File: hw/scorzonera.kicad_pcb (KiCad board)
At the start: 4 copper layers, 70.7 x 53.3 mm, 7 parts, among them J1 NEIGHBOR1, J2 NEIGHBOR2, J7 BONUS_ROW

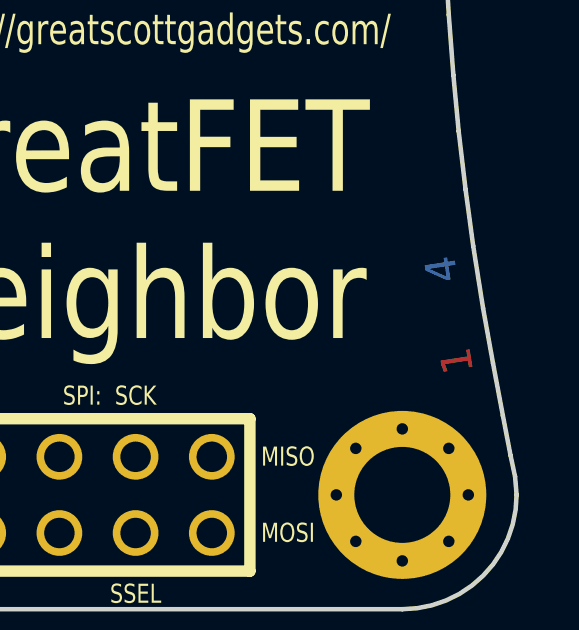
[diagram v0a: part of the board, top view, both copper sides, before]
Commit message: Switch to 2 layer
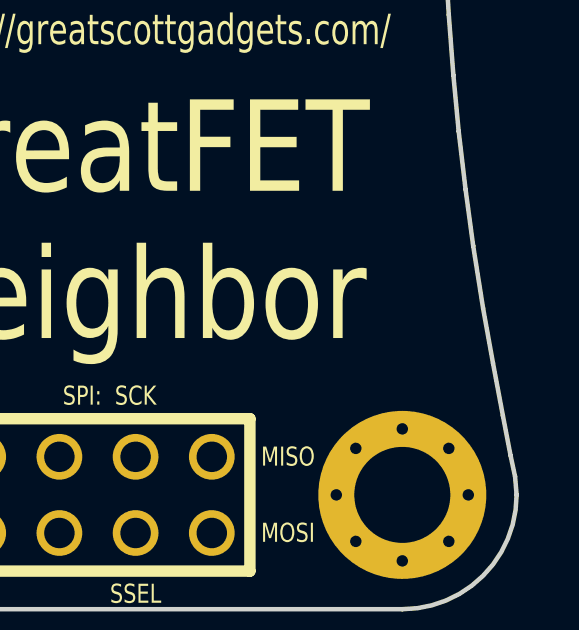
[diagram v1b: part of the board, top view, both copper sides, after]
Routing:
- removed copper zone on C2.Cu, net GND
- removed copper zone on C3.Cu, net VCC
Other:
- copper layers 4 -> 2
- board text removed: "1"
- board text removed: "2"
- board text removed: "3"
- board text removed: "4"
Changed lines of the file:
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@@
-(kicad_pcb (version 4) (host pcbnew 4.0.6)
+(kicad_pcb (version 20171130) (host pcbnew 5.0.2-bee76a0~70~ubuntu18.04.1)
   (general
-    (links 41)
-    (no_connects 0)
-    (area 107.95 66.04 279.525801 124.460001)
     (thickness 1.6)
-    (drawings 122)
+    (drawings 118)
     (tracks 0)
     (zones 0)
@@
   (layers
     (0 F.Cu signal)
-    (1 C2.Cu power)
-    (2 C3.Cu power)
     (31 B.Cu signal)
     (32 B.Adhes user)
@@
     (pad_drill 0.762)
     (pad_to_mask_clearance 0.127)
+    (solder_mask_min_width 0.25)
     (pad_to_paste_clearance_ratio -0.05)
     (aux_axis_origin 0 0)
@@
       (layerselection 0x010fc_80000007)
       (usegerberextensions true)
+      (usegerberattributes false)
+      (usegerberadvancedattributes false)
+      (creategerberjobfile false)
       (excludeedgelayer true)
       (linewidth 0.100000)
@@
       (hpglpennumber 1)
       (hpglpenspeed 20)
-      (hpglpendiameter 15)
-      (hpglpenoverlay 2)
+      (hpglpendiameter 15.000000)
       (psnegative false)
       (psa4output false)
@@
       (drillshape 0)
       (scaleselection 1)
-      (outputdirectory gerber))
+      (outputdirectory "gerber"))
   )
   (net 0 "")
@@
   (gr_text "27 September 2015" (at 153.4414 114.4016) (layer F.SilkS)
     (effects (font (size 1.016 0.762) (thickness 0.1524)))
-  )
-  (gr_text 4 (at 177.8508 110.5916 98.9) (layer B.Cu)
-    (effects (font (size 1.016 1.016) (thickness 0.1778)))
-  )
-  (gr_text 3 (at 178.0286 111.633 98.9) (layer C3.Cu)
-    (effects (font (size 1.016 1.016) (thickness 0.1778)))
-  )
-  (gr_text 2 (at 178.181 112.6236 98.9) (layer C2.Cu)
-    (effects (font (size 1.016 1.016) (thickness 0.1778)))
-  )
-  (gr_text 1 (at 178.3588 113.6396 98.9) (layer F.Cu)
-    (effects (font (size 1.016 1.016) (thickness 0.1778)))
   )
   (gr_text https://greatscottgadgets.com/ (at 168.021 102.616) (layer F.SilkS)
@@
   (gr_line (start 176.53 121.92) (end 116.1288 121.92) (angle 90) (layer Edge.Cuts) (width 0.15))
   (gr_line (start 116.1288 68.58) (end 176.53 68.58) (angle 90) (layer Edge.Cuts) (width 0.15))
-  (zone (net 2) (net_name VCC) (layer C3.Cu) (hatch edge 0.508)
-    (connect_pads (clearance 0.254))
-    (min_thickness 0.254)
-    (fill yes (arc_segments 16) (thermal_gap 0.254) (thermal_bridge_width 0.508))
-    (polygon
-      (pts
-        (xy 107.95 66.04) (xy 181.61 66.04) (xy 181.5084 109.0422) (xy 176.2506 109.8296) (xy 177.1142 114.7826)
-        (xy 181.61 114.0714) (xy 181.61 124.46) (xy 107.95 124.46)
-      )
-    )
-  )
-  (zone (net 1) (net_name GND) (layer C2.Cu) (hatch edge 0.508)
-    (connect_pads (clearance 0.254))
-    (min_thickness 0.254)
-    (fill yes (arc_segments 16) (thermal_gap 0.254) (thermal_bridge_width 0.508))
-    (polygon
-      (pts
-        (xy 107.95 66.04) (xy 181.61 66.04) (xy 181.5084 109.0422) (xy 176.2506 109.8296) (xy 177.1142 114.7826)
-        (xy 181.6354 114.0714) (xy 181.61 124.46) (xy 107.95 124.46)
-      )
-    )
-  )
 )

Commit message: Update silk
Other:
- board text added: "5 May 2019"
- board text added: "Scorzonera"
- board text added: "https://flomp.net/scorzonera"
- board text removed: "27 September 2015"
- board text removed: "GreatFET Neighbor"
- board text removed: "https://greatscottgadgets.com/"
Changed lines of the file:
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@@
   (gr_line (start 177.9016 92.3544) (end 177.8508 94.0054) (angle 90) (layer Edge.Cuts) (width 0.15))
   (gr_line (start 177.9524 90.5002) (end 177.9016 92.3544) (angle 90) (layer Edge.Cuts) (width 0.15))
-  (gr_text "27 September 2015" (at 153.4414 114.4016) (layer F.SilkS)
+  (gr_text "5 May 2019" (at 153.4414 114.4016) (layer F.SilkS)
     (effects (font (size 1.016 0.762) (thickness 0.1524)))
   )
-  (gr_text https://greatscottgadgets.com/ (at 168.021 102.616) (layer F.SilkS)
+  (gr_text https://flomp.net/scorzonera (at 168.1 105.3) (layer F.SilkS)
     (effects (font (size 1.016 0.762) (thickness 0.1524)))
   )
@@
   (gr_arc (start 176.53 118.11) (end 180.34 118.11) (angle 90) (layer Edge.Cuts) (width 0.15))
   (gr_arc (start 279.4508 95.25) (end 177.8508 95.25) (angle 12.5) (layer Cmts.User) (width 0.15))
-  (gr_text "GreatFET\nNeighbor" (at 167.386 109.0168) (layer F.SilkS)
+  (gr_text Scorzonera (at 167.386 109.0168) (layer F.SilkS)
     (effects (font (size 3.048 2.54) (thickness 0.4572)))
   )

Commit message: Some wiring
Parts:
- added U1: AM7969, Package_LCC:PLCC-28, F.Cu at (146.1, 92.1)
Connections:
- net /VBUS renamed Net-(J2-Pad2)
- J1 pad 10: (no net) -> /P1_1
- J1 pad 11: (no net) -> /CLK0
- J1 pad 12: (no net) -> /P1_2
- J1 pad 13: (no net) -> /P1_5
- J1 pad 14: (no net) -> /P5_2
- J1 pad 15: (no net) -> /P1_7
- J1 pad 16: (no net) -> /P1_6
- J1 pad 17: (no net) -> /P1_9
- J1 pad 18: (no net) -> /P1_8
- J1 pad 19: (no net) -> /P5_3
- J1 pad 20: (no net) -> /P1_10
- J1 pad 21: (no net) -> /P1_12
- J1 pad 22: (no net) -> /P1_11
- J1 pad 23: (no net) -> /P5_5
- J1 pad 24: (no net) -> /P5_4
- J1 pad 25: (no net) -> /P1_14
- J1 pad 26: (no net) -> /P1_13
- J1 pad 27: (no net) -> /P5_6
- J1 pad 28: (no net) -> /SGPIO2
- J1 pad 29: (no net) -> /P5_7
- J1 pad 3: (no net) -> /P4_9
- J1 pad 30: (no net) -> /SGPIO3
- J1 pad 31: (no net) -> /P1_18
- J1 pad 32: (no net) -> /P1_17
- J1 pad 33: (no net) -> /P9_5
- J1 pad 34: (no net) -> /P9_6
- J1 pad 35: (no net) -> /P2_0
- J1 pad 36: (no net) -> /P6_0
- J1 pad 37: (no net) -> /P1_20
- J1 pad 38: (no net) -> /P1_19
- J1 pad 39: (no net) -> /P1_4
- J1 pad 4: (no net) -> /SGPIO0
- J1 pad 40: (no net) -> /P1_3
- J1 pad 5: (no net) -> /P4_10
- J1 pad 6: (no net) -> /SGPIO1
- J1 pad 7: (no net) -> /P1_0
- J1 pad 8: (no net) -> /P5_0
- J1 pad 9: (no net) -> /P5_1
- J2 pad 10: (no net) -> /P4_6
- J2 pad 11: (no net) -> /P4_7
- J2 pad 12: (no net) -> /CLK2
- J2 pad 13: (no net) -> /P2_8
- J2 pad 14: (no net) -> /P2_7
- J2 pad 15: (no net) -> /P2_6
- J2 pad 16: (no net) -> /P7_7
- J2 pad 17: (no net) -> /WAKEUP0
- J2 pad 18: (no net) -> /P2_5
- J2 pad 19: (no net) -> /P2_4
- J2 pad 20: (no net) -> /P2_3
- J2 pad 21: (no net) -> /PF_4
- J2 pad 22: (no net) -> /P3_2
- J2 pad 23: (no net) -> /P7_2
- J2 pad 24: (no net) -> /P3_1
- J2 pad 25: (no net) -> /P7_1
- J2 pad 26: (no net) -> /P3_0
- J2 pad 27: (no net) -> /SGPIO4
- J2 pad 28: (no net) -> /P3_4
- J2 pad 29: (no net) -> /SGPIO7
- J2 pad 3: (no net) -> /P4_8
- J2 pad 30: (no net) -> /P3_7
- J2 pad 31: (no net) -> /SGPIO6
- J2 pad 32: (no net) -> /P3_3
- J2 pad 33: (no net) -> /P2_2
- J2 pad 34: (no net) -> /SGPIO5
- J2 pad 35: (no net) -> /P2_1
- J2 pad 36: (no net) -> /P6_3
- J2 pad 37: (no net) -> /P3_5
- J2 pad 38: (no net) -> /P3_6
- J2 pad 39: (no net) -> /I2C0_SDA
- J2 pad 4: (no net) -> /P4_0
- J2 pad 40: (no net) -> /I2C0_SCL
- J2 pad 5: (no net) -> /ADC0_0
- J2 pad 6: (no net) -> /P4_5
- J2 pad 7: (no net) -> /P4_4
- J2 pad 8: (no net) -> /P4_2
- J2 pad 9: (no net) -> /P4_3
- J7 pad 11: (no net) -> /RESET
- J7 pad 12: (no net) -> /VBAT
- J7 pad 13: (no net) -> /P2_11
- J7 pad 14: (no net) -> /P2_10
- J7 pad 15: (no net) -> /P6_10
- J7 pad 16: (no net) -> /P6_9
- J7 pad 17: (no net) -> /P6_2
- J7 pad 18: (no net) -> /P6_1
- J7 pad 2: (no net) -> /P6_4
- J7 pad 3: (no net) -> /P6_5
- J7 pad 4: (no net) -> /ADC0_5
- J7 pad 5: (no net) -> /ADC0_2
- J7 pad 6: (no net) -> /P2_9
- J7 pad 7: (no net) -> /P2_12
- J7 pad 8: (no net) -> /P2_13
- J7 pad 9: (no net) -> /RTC_ALARM

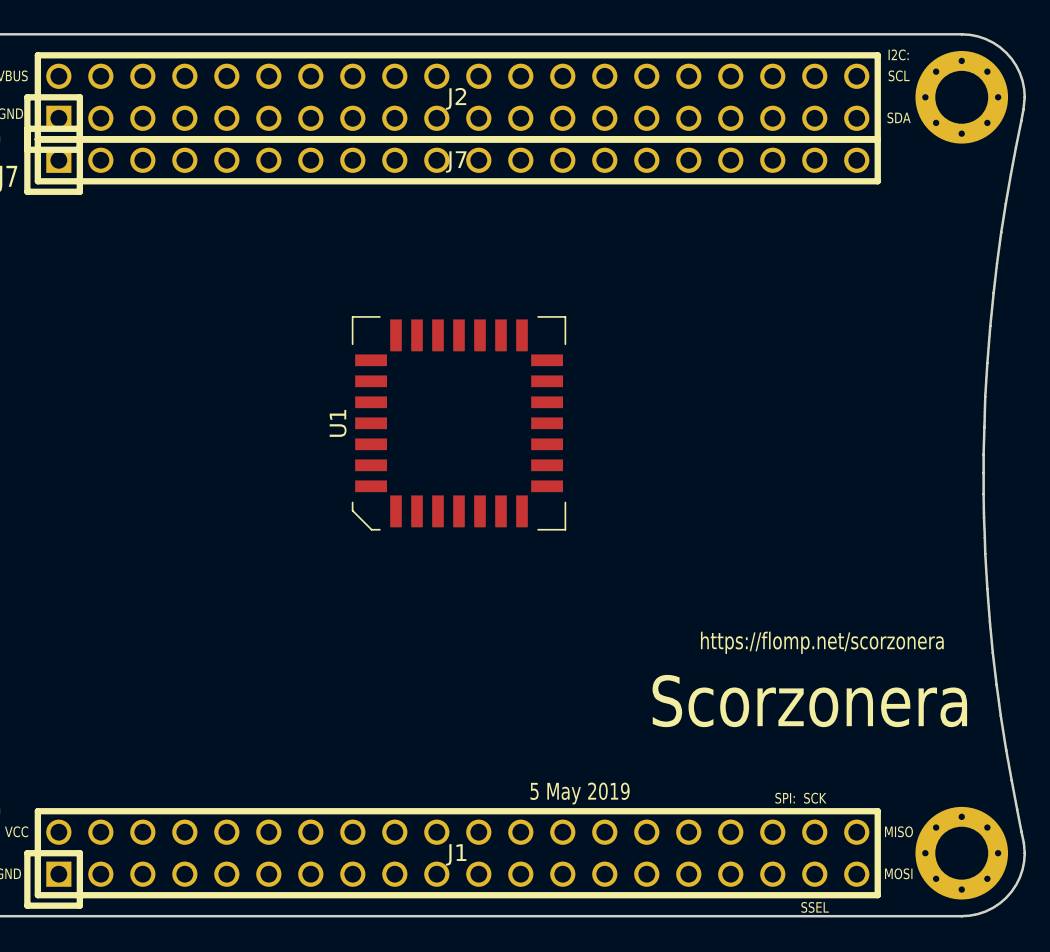
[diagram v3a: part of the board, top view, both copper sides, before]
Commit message: Map out remaining SGPIO, add SERIN dividers, etc.
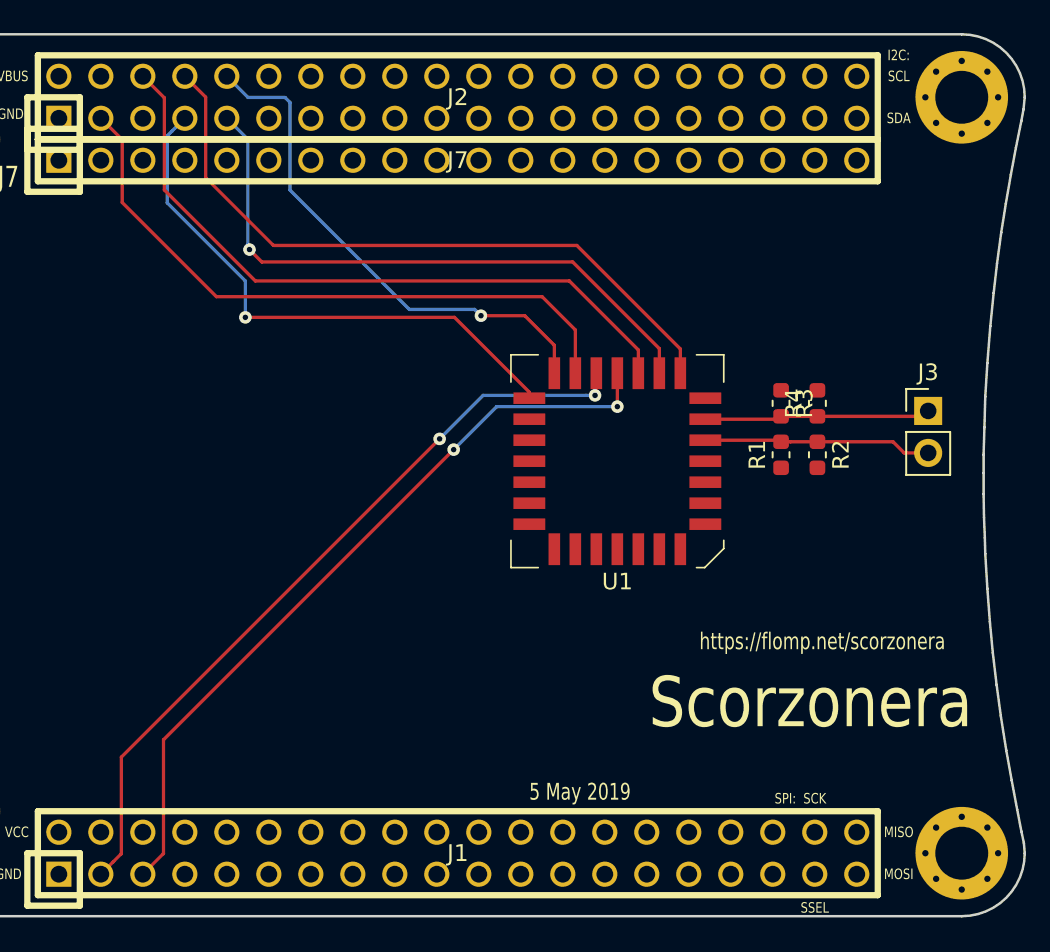
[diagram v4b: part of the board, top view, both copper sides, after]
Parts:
- added J3: Conn_01x02, Connector_PinHeader_2.54mm:PinHeader_1x02_P2.54mm_Vertical, F.Cu at (174.5, 91.4)
- added R1: 120R, Resistor_SMD:R_0603_1608Metric, F.Cu at (165.6, 94.0)
- added R2: 330R, Resistor_SMD:R_0603_1608Metric, F.Cu at (167.8, 94.0)
- added R3: 120R, Resistor_SMD:R_0603_1608Metric, F.Cu at (165.6, 90.9)
- added R4: 330R, Resistor_SMD:R_0603_1608Metric, F.Cu at (167.8, 90.9)
- moved U1 9.85 mm to (155.7, 94.4), turned to 180 degrees
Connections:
- J1 pad 3: /P4_9 -> /SGPIO14
- J1 pad 5: /P4_10 -> /SGPIO15
- J2 pad 10: /P4_6 -> /SGPIO12
- J2 pad 3: /P4_8 -> /SGPIO13
- J2 pad 6: /P4_5 -> /SGPIO11
- J2 pad 7: /P4_4 -> /SGPIO10
- J2 pad 8: /P4_2 -> /SGPIO8
- J2 pad 9: /P4_3 -> /SGPIO9
- U1 pad 10: Net-(U1-Pad10) -> /SERIN-
- U1 pad 12: Net-(U1-Pad12) -> /SGPIO8
- U1 pad 13: Net-(U1-Pad13) -> /SGPIO9
- U1 pad 14: Net-(U1-Pad14) -> /SGPIO11
- U1 pad 15: Net-(U1-Pad15) -> /SGPIO15
- U1 pad 16: Net-(U1-Pad16) -> /SGPIO14
- U1 pad 17: Net-(U1-Pad17) -> /SGPIO13
- U1 pad 18: Net-(U1-Pad18) -> /SGPIO12
- U1 pad 19: Net-(U1-Pad19) -> /SGPIO10
- U1 pad 24: Net-(U1-Pad24) -> /SGPIO10
- U1 pad 9: Net-(U1-Pad9) -> /SERIN+
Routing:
- net /SGPIO14: track 0.00 -> 46.7 mm, vias 0 -> 2
- net /SGPIO15: track 0.00 -> 46.5 mm, vias 0 -> 2
- net /SGPIO11: track 0.00 -> 41.5 mm
- net /SGPIO8: track 0.00 -> 41.1 mm
- net /SGPIO13: track 0.00 -> 38.8 mm
- net /SGPIO9: track 0.00 -> 37.3 mm, vias 0 -> 1
- net /SGPIO10: track 0.00 -> 33.9 mm, vias 0 -> 1
- net /SGPIO12: track 0.00 -> 31.3 mm, vias 0 -> 1
- net /SERIN+: track 0.00 -> 13.8 mm
- net /SERIN-: track 0.00 -> 13.7 mm
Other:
- net class Default: clearance 0.1524 -> 0.2; trace_width 0.2032 -> 0.2
- rule trace_clearance: 0.1524 -> 0.2
- rule trace_min: 0.2032 -> 0.15

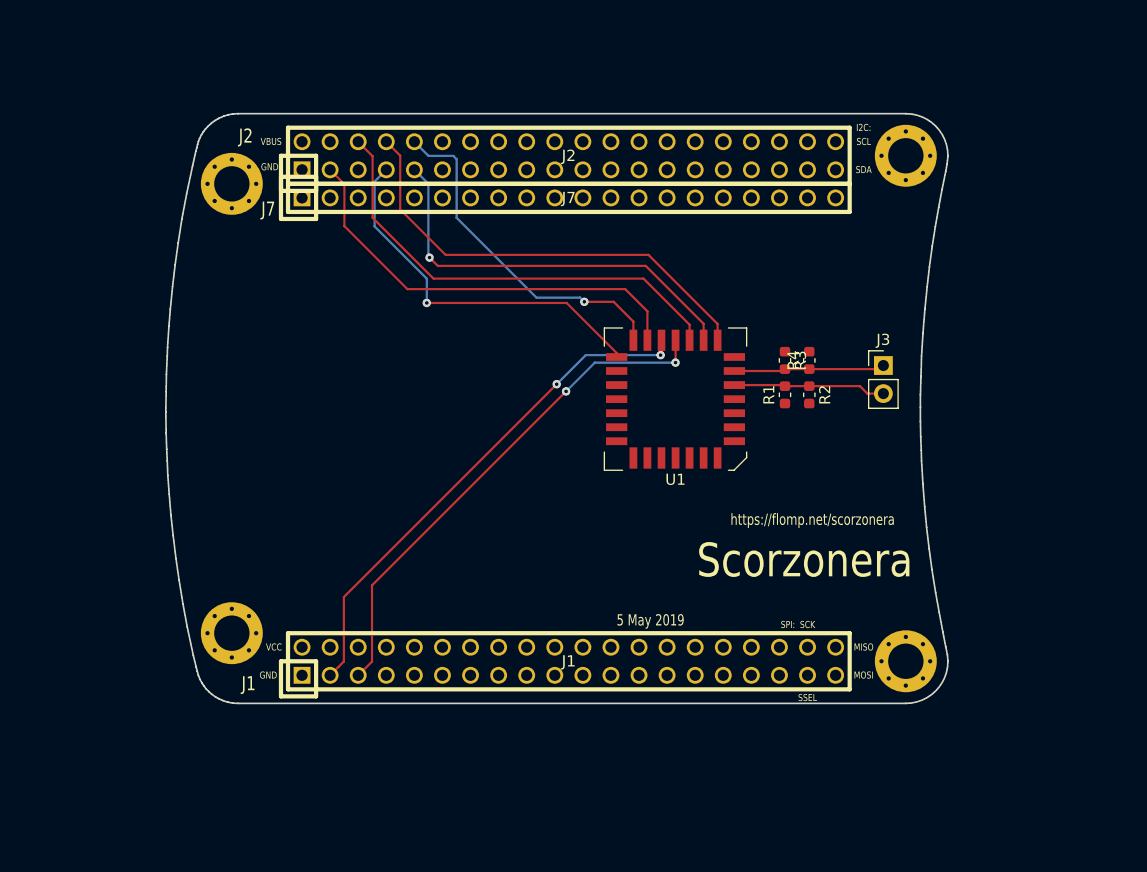
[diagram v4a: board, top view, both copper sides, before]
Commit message: Level translator and some routing
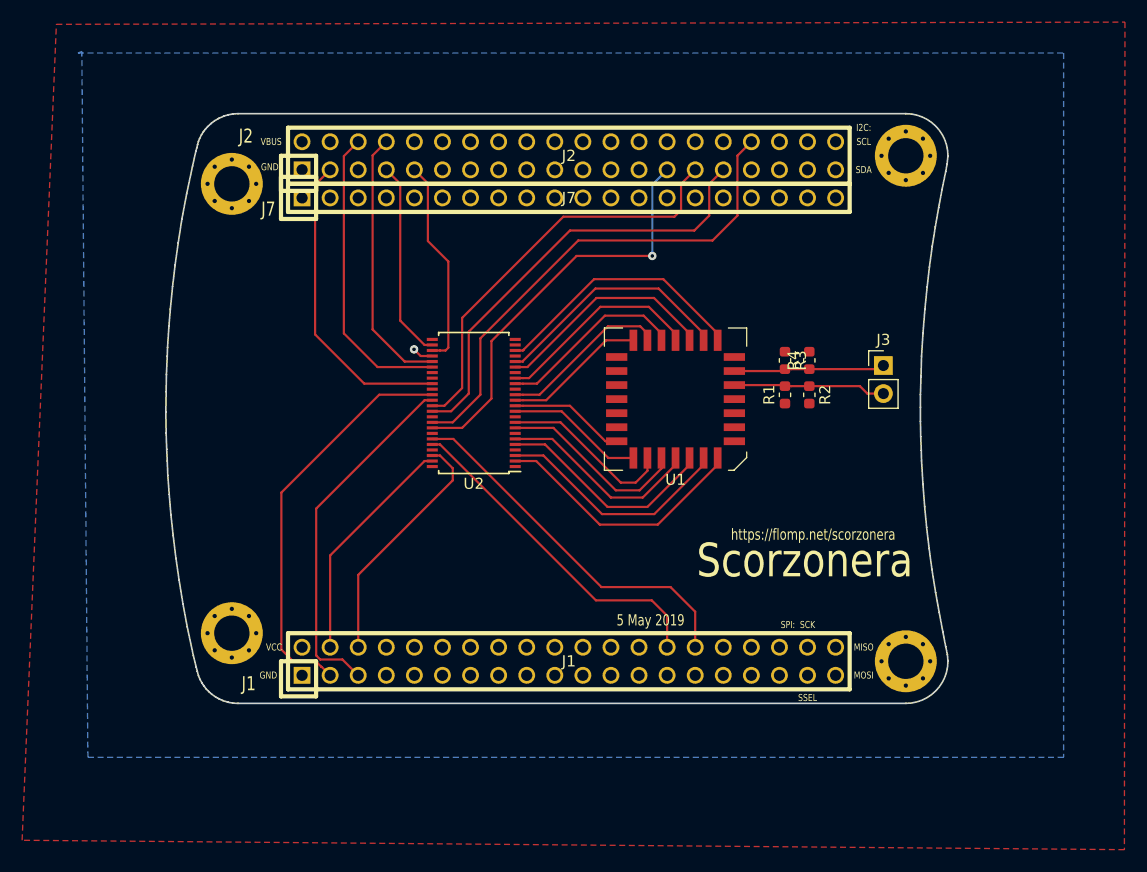
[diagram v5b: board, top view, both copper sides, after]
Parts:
- added U2: 74ALVC164245, Package_SO:TSSOP-48_6.1x12.5mm_P0.5mm, F.Cu at (137.4, 94.8)
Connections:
- J2 pad 2: Net-(J2-Pad2) -> +5V
- U1 pad 1: /SGPIO3 -> /DO3
- U1 pad 11: Net-(U1-Pad11) -> GND
- U1 pad 12: /SGPIO8 -> /DSTRB
- U1 pad 13: /SGPIO9 -> /CSTRB
- U1 pad 14: /SGPIO11 -> /VLTN
- U1 pad 15: /SGPIO15 -> /CO0
- U1 pad 16: /SGPIO14 -> /CO1
- U1 pad 17: /SGPIO13 -> /CO2
- U1 pad 18: /SGPIO12 -> /CO3
- U1 pad 19: /SGPIO10 -> /CLK
- U1 pad 2: /SGPIO2 -> /DO2
- U1 pad 24: /SGPIO10 -> /CLK
- U1 pad 25: /SGPIO7 -> /DO7
- U1 pad 26: /SGPIO6 -> /DO6
- U1 pad 27: /SGPIO5 -> /DO5
- U1 pad 28: /SGPIO4 -> /DO4
- U1 pad 3: /SGPIO1 -> /DO1
- U1 pad 4: /SGPIO0 -> /DO0
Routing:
- net /SGPIO5: track 0.00 -> 45.5 mm
- net /SGPIO6: track 0.00 -> 40.3 mm
- net /SGPIO4: track 0.00 -> 37.7 mm, vias 0 -> 1
- net /SGPIO7: track 0.00 -> 37.7 mm
- net /SGPIO3: track 0.00 -> 33.5 mm
- net /SGPIO12: track 31.3 -> 0.00 mm, vias 1 -> 0
- net /SGPIO2: track 0.00 -> 30.5 mm
- net /DSTRB: track 0.00 -> 23.6 mm
- net /DO0: track 0.00 -> 23.5 mm
- net /CSTRB: track 0.00 -> 22.1 mm
- net /SGPIO1: track 0.00 -> 22.1 mm
- net /DO1: track 0.00 -> 21.7 mm
- net /SGPIO0: track 0.00 -> 21.1 mm
- net /DO2: track 0.00 -> 20.3 mm
- net /VLTN: track 0.00 -> 20.3 mm
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- added copper zone on B.Cu, net GND
- added copper zone on F.Cu, net GND

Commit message: Routed! for now
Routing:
- net +5V: track 0.00 -> 96.5 mm, vias 0 -> 4
- net VCC: track 0.00 -> 82.6 mm, vias 0 -> 3
- net /SGPIO12: track 0.00 -> 26.9 mm
- net GND: track 1.90 -> 22.8 mm, vias 1 -> 8
- net /CLK: track 0.00 -> 20.1 mm, vias 0 -> 3
- net /SGPIO15: track 32.4 -> 34.0 mm
- net /SGPIO5: track 45.5 -> 47.0 mm
- net /SGPIO4: track 37.7 -> 39.2 mm

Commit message: RS232
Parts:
- added J4: Conn_01x02, Connector_PinHeader_2.54mm:PinHeader_1x02_P2.54mm_Vertical, F.Cu at (174.6, 83.7)
- added U3: MAX3232, Package_SO:TSSOP-16_4.4x5mm_P0.65mm, F.Cu at (167.7, 82.2)
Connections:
- J2 pad 28: /P3_4 -> /U1_TXD
- J2 pad 37: /P3_5 -> /U1_RXD
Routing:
- net /U1_TXD: track 0.00 -> 22.6 mm
- net GND: track 22.8 -> 39.5 mm, vias 8 -> 13
- net /U1_RXD: track 0.00 -> 9.97 mm
- net VCC: track 82.6 -> 86.9 mm, vias 3 -> 4
- net /CO2: track 15.4 -> 16.2 mm
